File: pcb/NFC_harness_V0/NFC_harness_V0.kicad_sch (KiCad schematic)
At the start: 33 parts, among them J1 armed, J2 programmer, J3 Vin, J4 triggerd, J5 sender, J6 detector, J7 triggerd, Q1 MMBT3904, U1 ATtiny202-SS, U4 TPS613221ADBV

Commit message: initial commit - with tiny, will be changed to pico
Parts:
- removed C1, C2, C5, C9: 100n, Capacitor_SMD:C_0805_2012Metric, symbol Device:C
- removed C14: 4.7u, Capacitor_SMD:C_1206_3216Metric, symbol Device:C
- removed C3: 10u, Capacitor_SMD:C_0805_2012Metric, symbol Device:C
- removed D1, D2: LED, LED_SMD:LED_1206_3216Metric, symbol Device:LED
- removed J1: armed, Connector_PinHeader_2.54mm:PinHeader_1x02_P2.54mm_Vertical, symbol Connector:Conn_01x02_Pin
- removed J2: programmer, Connector_PinHeader_2.54mm:PinHeader_1x03_P2.54mm_Vertical, symbol Connector:Conn_01x03_Pin
- removed J4, J7: triggerd, Connector_PinHeader_2.54mm:PinHeader_1x02_P2.54mm_Vertical, symbol Connector:Conn_01x02_Pin
- removed J5: sender, Connector_PinHeader_2.54mm:PinHeader_1x03_P2.54mm_Vertical, symbol Connector:Conn_01x03_Pin
- removed J6: detector, Connector_PinHeader_2.54mm:PinHeader_1x03_P2.54mm_Vertical, symbol Connector:Conn_01x03_Pin
- removed L1: 6.8 uH, Inductor Coilcraft:L_Coilcraft_LPS4018, symbol Device:L
- removed Q1: MMBT3904, Package_TO_SOT_SMD:SOT-23, symbol Transistor_BJT:MMBT3904
- removed R1: 1k, Resistor_SMD:R_0805_2012Metric, symbol Device:R
- removed R11, R9: 470k, Resistor_SMD:R_0805_2012Metric, symbol Device:R
- removed R2, R3, R7: 220, Resistor_SMD:R_0805_2012Metric, symbol Device:R
- removed R4, R5: 100k, Resistor_SMD:R_0805_2012Metric, symbol Device:R
- removed R6: 1M, Resistor_SMD:R_0805_2012Metric, symbol Device:R
- removed U1: ATtiny202-SS, Package_SO:SOIC-8_3.9x4.9mm_P1.27mm, symbol MCU_Microchip_ATtiny:ATtiny202-SS
- removed U4: TPS613221ADBV, Package_TO_SOT_SMD:SOT-23-5, symbol Regulator_Switching:TPS613221ADBV
- added A1: RaspberryPi_Pico_W, Module_RaspberryPi_Pico:RaspberryPi_Pico_W_SMD, symbol MCU_Module_RaspberryPi_Pico:RaspberryPi_Pico_W_DebugPins
- added SW1: SW_DIP_x04, symbol Switch:SW_DIP_x04
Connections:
- new net: A1.13 (GND), A1.18 (GND), A1.23 (GND), A1.28 (GND), A1.3 (GND), A1.38 (GND), A1.8 (GND), A1.D2 (GND)

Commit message: pcb symbols st25
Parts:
- added IC1: ST25DV04KC-IE6S3, ST25DV04KC-IE6S3:SOIC127P600X175-8N, symbol ST25DV04KC-IE6S3:ST25DV04KC-IE6S3
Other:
- moved on the sheet: SW1
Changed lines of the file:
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@@
 	(symbol
 		(lib_id "Switch:SW_DIP_x04")
-		(at 135.89 119.38 0)
+		(at 189.23 96.52 0)
 		(unit 1)
 		(exclude_from_sim no)
@@
 		(fields_autoplaced yes)
 		(property "Reference" "SW1"
-			(at 135.89 106.68 0)
+			(at 189.23 83.82 0)
 			(effects
 				(font
@@
 		)
 		(property "Value" "SW_DIP_x04"
-			(at 135.89 109.22 0)
+			(at 189.23 86.36 0)
 			(effects
 				(font
@@
 		)
 		(property "Footprint" ""
-			(at 135.89 119.38 0)
+			(at 189.23 96.52 0)
 			(effects
 				(font
@@
 		)
 		(property "Datasheet" "~"
-			(at 135.89 119.38 0)
+			(at 189.23 96.52 0)
 			(effects
 				(font
@@
 		)
 		(property "Description" "4x DIP Switch, Single Pole Single Throw (SPST) switch, small symbol"
-			(at 135.89 119.38 0)
+			(at 189.23 96.52 0)
 			(effects
 				(font
@@
 					(unit 1)
 				)
+			)
+		)
+	)
+	(symbol
+		(lib_id "ST25DV04KC-IE6S3:ST25DV04KC-IE6S3")
+		(at 120.65 74.93 0)
+		(unit 1)
+		(exclude_from_sim no)
+		(in_bom yes)
+		(on_board yes)
+		(dnp no)
+		(fields_autoplaced yes)
+		(property "Reference" "IC1"
+			(at 142.24 67.31 0)
+			(effects
+				(font
+					(size 1.27 1.27)
+				)
+			)
+		)
+		(property "Value" "ST25DV04KC-IE6S3"
+			(at 142.24 69.85 0)
+			(effects
+				(font
+					(size 1.27 1.27)
+				)
+			)
+		)
+		(property "Footprint" "ST25DV04KC-IE6S3:SOIC127P600X175-8N"
+			(at 160.02 169.85 0)
+			(effects
+				(font
+					(size 1.27 1.27)
+				)
+				(justify left top)
+				(hide yes)
+			)
+		)
+		(property "Datasheet" "https://www.st.com/resource/en/datasheet/st25dv04kc.pdf"
+			(at 160.02 269.85 0)
+			(effects
+				(font
+					(size 1.27 1.27)
+				)
+				(justify left top)
+				(hide yes)
+			)
+		)
+		(property "Description" "Dynamic NFC/RFID tag IC with 4-, 16-, or 64-Kbit EEPROM, fast transfer mode capability, and optimized I2C"
+			(at 120.65 74.93 0)
+			(effects
+				(font
+					(size 1.27 1.27)
+				)
+				(hide yes)
+			)
+		)
+		(property "Height" "1.75"
+			(at 160.02 469.85 0)
+			(effects
+				(font
+					(size 1.27 1.27)
+				)
+				(justify left top)
+				(hide yes)
+			)
+		)
+		(property "Mouser Part Number" "511-ST25DV04KC-IE6S3"
+			(at 160.02 569.85 0)
+			(effects
+				(font
+					(size 1.27 1.27)
+				)
+				(justify left top)
+				(hide yes)
+			)
+		)
+		(property "Mouser Price/Stock" "https://www.mouser.co.uk/ProductDetail/STMicroelectronics/ST25DV04KC-IE6S3?qs=QNEnbhJQKvZQBnG6g7VtqA%3D%3D"
+			(at 160.02 669.85 0)
+			(effects
+				(font
+					(size 1.27 1.27)
+				)
+				(justify left top)
+				(hide yes)
+			)
+		)
+		(property "Manufacturer_Name" "STMicroelectronics"
+			(at 160.02 769.85 0)
+			(effects
+				(font
+					(size 1.27 1.27)
+				)
+				(justify left top)
+				(hide yes)
+			)
+		)
+		(property "Manufacturer_Part_Number" "ST25DV04KC-IE6S3"
+			(at 160.02 869.85 0)
+			(effects
+				(font
+					(size 1.27 1.27)
+				)
+				(justify left top)
+				(hide yes)
+			)
+		)
+		(pin "2"
+		)
+		(pin "1"
+		)
+		(pin "5"
+		)
+		(pin "3"
+		)
+		(pin "6"
+		)
+		(pin "7"
+		)
+		(pin "4"
+		)
+		(pin "8"
+		)
+		(instances
+			(project ""
+				(path "/c4720908-7c6f-4e13-a46e-cd0970db3513"
+					(reference "IC1")
+					(unit 1)
+				)

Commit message: pcb work
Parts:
- removed C4: 100n, Capacitor_SMD:C_0805_2012Metric, symbol Device:C
- removed C6: 10u, Capacitor_SMD:C_0805_2012Metric, symbol Device:C
- removed H1: MountingHole, MountingHole:MountingHole_2.1mm, symbol Mechanical:MountingHole
- removed R10, R8: 0, Resistor_SMD:R_1206_3216Metric, symbol Device:R
- removed SW1: SW_DIP_x04, symbol Switch:SW_DIP_x04
- added C1: 100n, Capacitor_SMD:C_0805_2012Metric, symbol Device:C
- added R1, R2: 4k7, Resistor_SMD:R_1206_3216Metric, symbol Device:R
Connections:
- net GND: now also A1.13 (GND), A1.18 (GND), A1.23 (GND), A1.28 (GND), A1.3 (GND), A1.33 (AGND), A1.38 (GND), A1.8 (GND), A1.D2 (GND), IC1.4 (VSS), C1.2; no longer J3.1 (Pin_1)
- net at J3.2 (Pin_2): now also IC1.3 (AC1)
- net at IC1.2 (AC0): now also J3.1 (Pin_1)
- net at IC1.5 (SDA): now also A1.26 (GPIO20), R1.2
- net at IC1.6 (SCL): now also A1.27 (GPIO21), R2.2
- net at IC1.7 (GPO_(OPEN_DRAIN)): now also A1.25 (GPIO19)
- net at IC1.8 (VCC): now also A1.24 (GPIO18), C1.1
- net at A1.36 (3V3): now also R1.1, R2.1
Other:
- moved on the sheet: IC1, J3

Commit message: cam job output
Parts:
- added C13, C4: 4.7u, Capacitor_SMD:C_1206_3216Metric, symbol Device:C
- added C2: 10p, Capacitor_SMD:C_0805_2012Metric, symbol Device:C
- added C3: JZ400, JZ400:JZ400, symbol JZ400:JZ400
- added J1: energy harvest, Connector_PinHeader_2.54mm:PinHeader_1x02_P2.54mm_Vertical, symbol Connector:Conn_01x02_Pin
- added R3: 0, Resistor_SMD:R_1206_3216Metric, symbol Device:R
- J3: value Vin -> antenna
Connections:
- net GND: now also C13.2, C4.2, J1.1 (Pin_1), R3.1, R3.2
- net at IC1.1 (V_EH): now also C13.1, J1.2 (Pin_2)
- net at IC1.2 (AC0), J3.1 (Pin_1): now also C2.2, C3.1
- net at IC1.3 (AC1), J3.2 (Pin_2): now also C2.1, C3.2
- net at A1.24 (GPIO18), C1.1, IC1.8 (VCC): now also C4.1
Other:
- moved on the sheet: J3

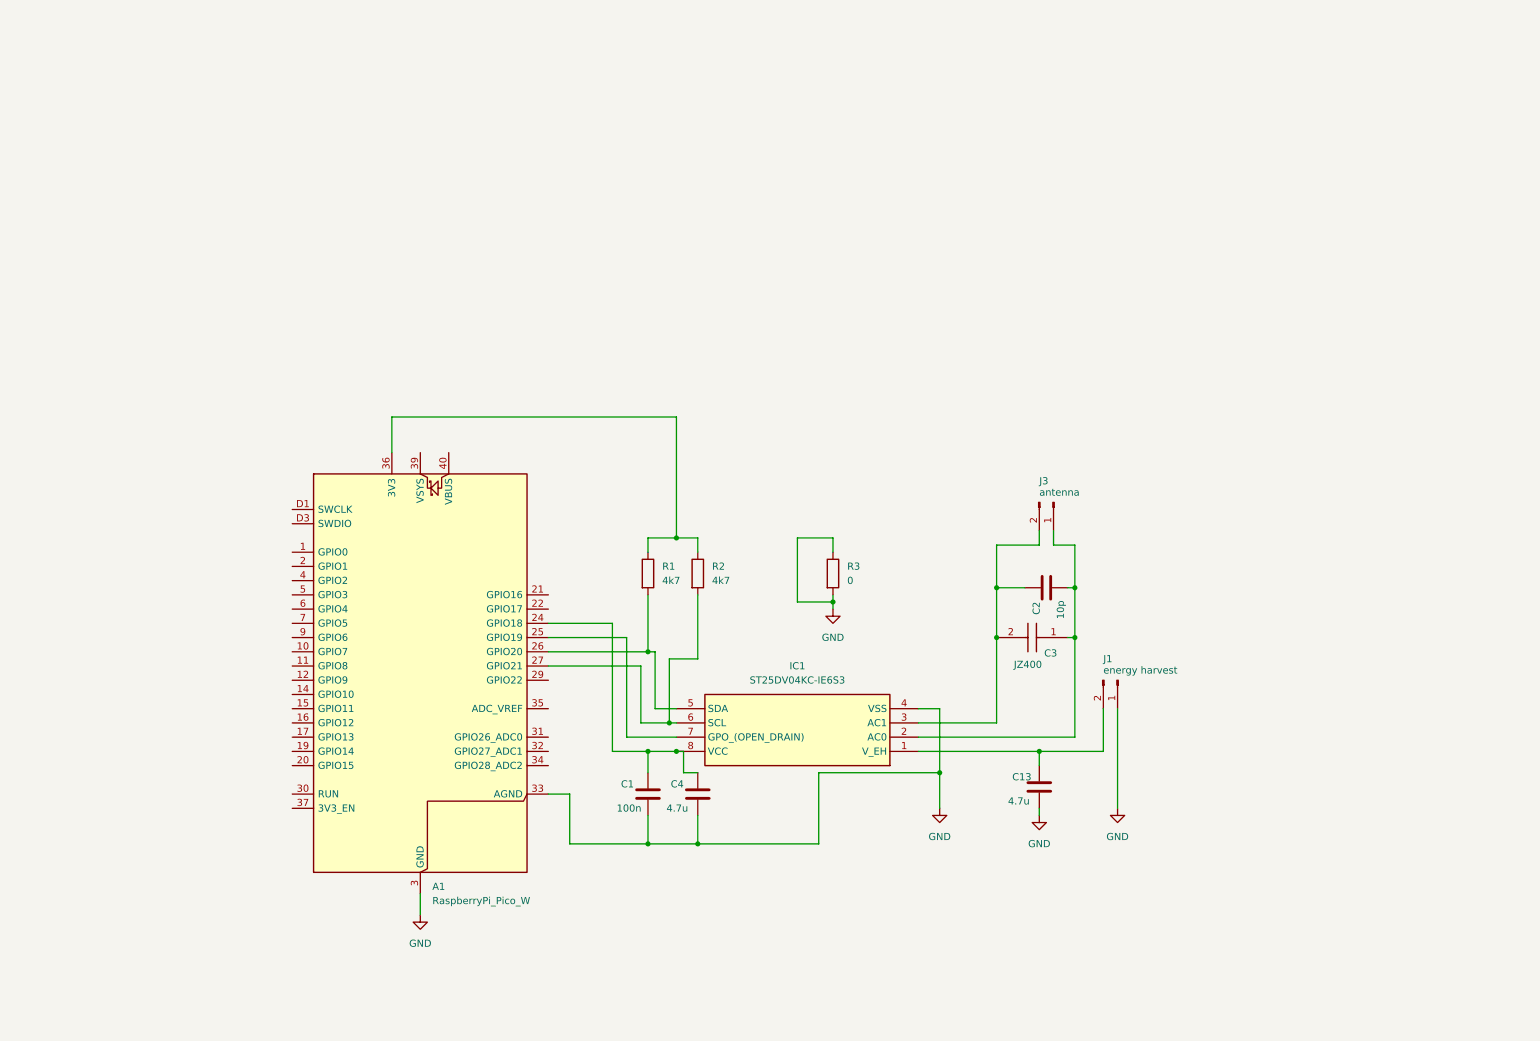
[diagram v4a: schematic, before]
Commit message: pcb: update NFC harness and add Taster 9313 footprint
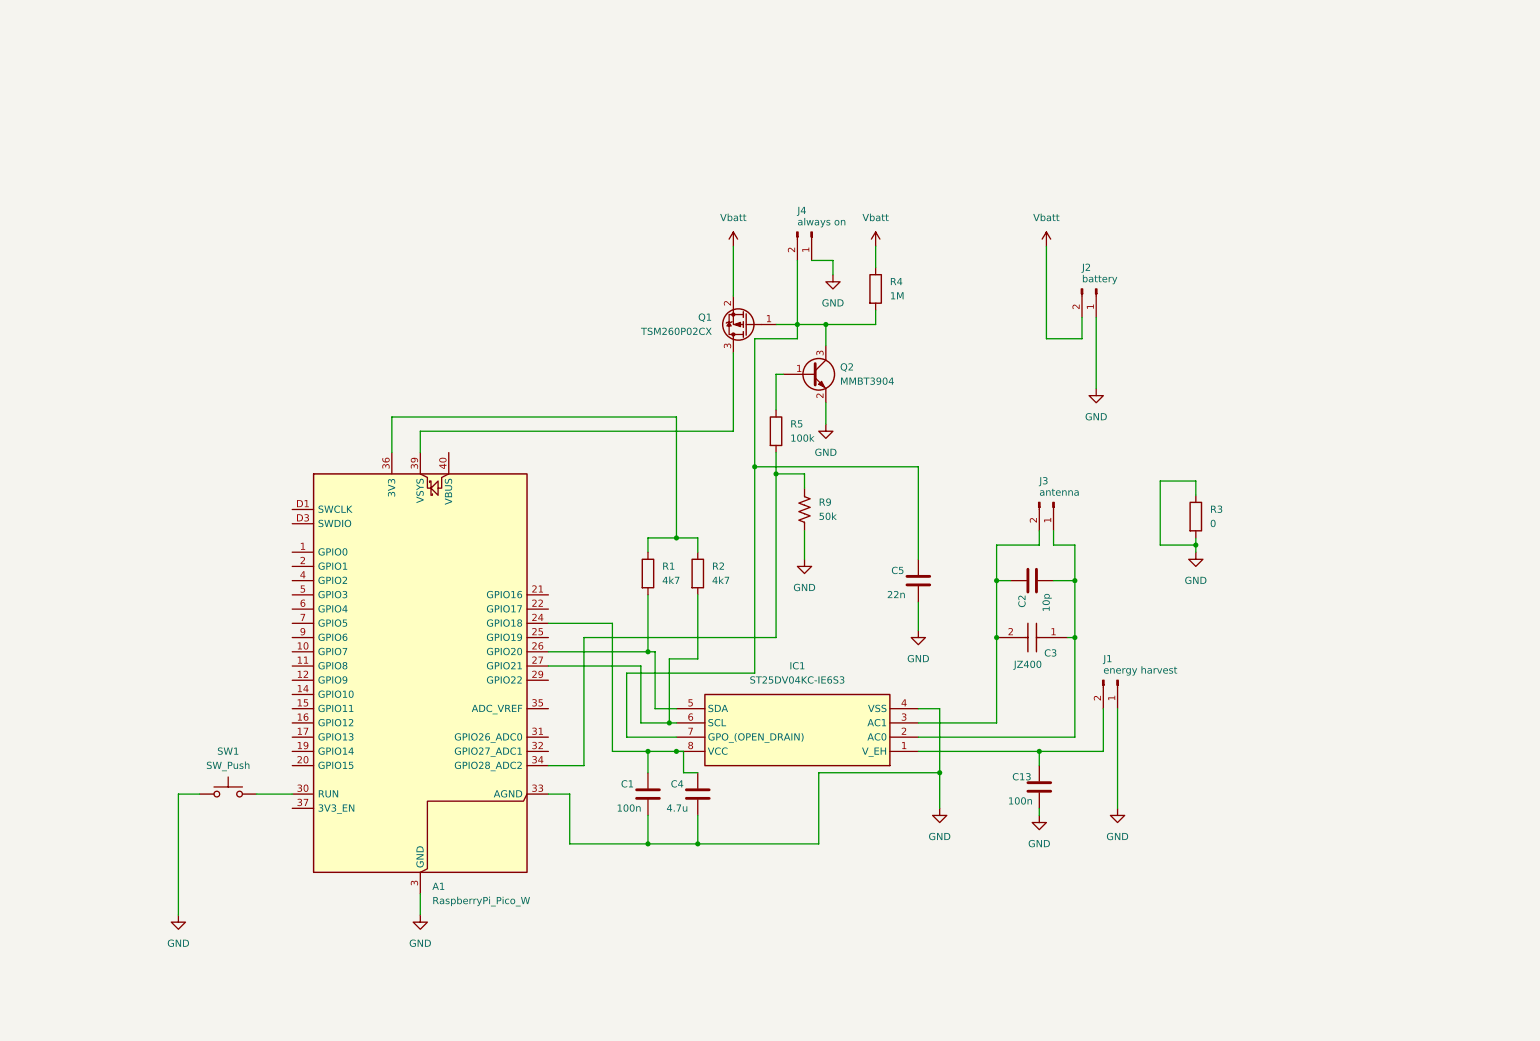
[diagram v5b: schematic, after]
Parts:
- added C5: 22n, Capacitor_SMD:C_0805_2012Metric, symbol Device:C
- added J2: battery, Connector_PinHeader_2.54mm:PinHeader_1x02_P2.54mm_Vertical, symbol Connector:Conn_01x02_Pin
- added J4: always on, Connector_PinHeader_2.54mm:PinHeader_1x02_P2.54mm_Vertical, symbol Connector:Conn_01x02_Pin
- added Q1: TSM260P02CX, Package_TO_SOT_SMD:SOT-23_Handsoldering, symbol Transistor_FET:TSM2301ACX
- added Q2: MMBT3904, Package_TO_SOT_SMD:SOT-23, symbol Transistor_BJT:MMBT3904
- added R4: 1M, Resistor_SMD:R_0805_2012Metric_Pad1.20x1.40mm_HandSolder, symbol Device:R
- added R5: 100k, Fuse:Fuse_1206_3216Metric_Pad1.42x1.75mm_HandSolder, symbol Device:R
- added R9: 50k, Fuse:Fuse_1206_3216Metric_Pad1.42x1.75mm_HandSolder, symbol Device:R_US
- added SW1: SW_Push, Taster:Taster 9313, symbol Switch:SW_Push
- C13: value 4.7u -> 100n; footprint Capacitor_SMD:C_1206_3216Metric -> Capacitor_SMD:C_0805_2012Metric
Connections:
- net GND: now also C5.2, J2.1 (Pin_1), J4.1 (Pin_1), Q2.2 (E), R9.2, SW1.1
- net at IC1.7 (GPO_(OPEN_DRAIN)): now also C5.1, J4.2 (Pin_2), Q1.1 (G), Q2.3 (C), R4.2; no longer A1.25 (GPIO19)
- net at A1.30 (RUN): now also SW1.2
- net at A1.34 (GPIO28_ADC2): now also R5.2, R9.1
- net at A1.39 (VSYS): now also Q1.3 (D)
- new net: Q2.1 (B), R5.1
- new net Vbatt: J2.2 (Pin_2), Q1.2 (S), R4.1
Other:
- moved on the sheet: C2, R3

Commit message: pcb edits
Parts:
- added R6: 0, Fuse:Fuse_1206_3216Metric_Pad1.42x1.75mm_HandSolder, symbol Device:R
- R1, R2, R3: footprint Resistor_SMD:R_1206_3216Metric -> Fuse:Fuse_1206_3216Metric_Pad1.42x1.75mm_HandSolder
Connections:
- net GND: now also R6.1, R6.2
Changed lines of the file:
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@@
 	)
 	(junction
+		(at 227.33 97.79)
+		(diameter 0)
+		(color 0 0 0 0)
+	)
+	(junction
 		(at 191.77 125.73)
 		(diameter 0)
@@
 	(wire
 		(pts
+			(xy 234.95 100.33) (xy 234.95 97.79)
+		)
+		(stroke
+			(width 0)
+			(type default)
+		)
+	)
+	(wire
+		(pts
 			(xy 138.43 162.56) (xy 160.02 162.56)
 		)
@@
 	(wire
 		(pts
+			(xy 227.33 109.22) (xy 234.95 109.22)
+		)
+		(stroke
+			(width 0)
+			(type default)
+		)
+	)
+	(wire
+		(pts
 			(xy 59.69 153.67) (xy 66.04 153.67)
 		)
@@
 	(wire
 		(pts
+			(xy 234.95 97.79) (xy 227.33 97.79)
+		)
+		(stroke
+			(width 0)
+			(type default)
+		)
+	)
+	(wire
+		(pts
 			(xy 161.29 83.82) (xy 161.29 87.63)
 		)
@@
 	(wire
 		(pts
+			(xy 234.95 109.22) (xy 234.95 107.95)
+		)
+		(stroke
+			(width 0)
+			(type default)
+		)
+	)
+	(wire
+		(pts
 			(xy 130.81 128.27) (xy 130.81 138.43)
 		)
@@
 			)
 		)
-		(property "Footprint" "Resistor_SMD:R_1206_3216Metric"
+		(property "Footprint" "Fuse:Fuse_1206_3216Metric_Pad1.42x1.75mm_HandSolder"
 			(at 225.552 104.14 90)
 			(effects
@@
 			)
 		)
-		(property "Footprint" "Resistor_SMD:R_1206_3216Metric"
+		(property "Footprint" "Fuse:Fuse_1206_3216Metric_Pad1.42x1.75mm_HandSolder"
 			(at 136.652 114.3 90)
 			(effects
@@
 	)
 	(symbol
+		(lib_id "Device:R")
+		(at 234.95 104.14 0)
+		(unit 1)
+		(exclude_from_sim no)
+		(in_bom yes)
+		(on_board yes)
+		(dnp no)
+		(fields_autoplaced yes)
+		(property "Reference" "R6"
+			(at 237.49 102.8699 0)
+			(effects
+				(font
+					(size 1.27 1.27)
+				)
+				(justify left)
+			)
+		)
+		(property "Value" "0"
+			(at 237.49 105.4099 0)
+			(effects
+				(font
+					(size 1.27 1.27)
+				)
+				(justify left)
+			)
+		)
+		(property "Footprint" "Fuse:Fuse_1206_3216Metric_Pad1.42x1.75mm_HandSolder"
+			(at 233.172 104.14 90)
+			(effects
+				(font
+					(size 1.27 1.27)
+				)
+				(hide yes)
+			)
+		)
+		(property "Datasheet" "~"
+			(at 234.95 104.14 0)
+			(effects
+				(font
+					(size 1.27 1.27)
+				)
+				(hide yes)
+			)
+		)
+		(property "Description" "Resistor"
+			(at 234.95 104.14 0)
+			(effects
+				(font
+					(size 1.27 1.27)
+				)
+				(hide yes)
+			)
+		)
+		(pin "2"
+		)
+		(pin "1"
+		)
+		(instances
+			(project "NFC_harness_V0"
+				(path "/c4720908-7c6f-4e13-a46e-cd0970db3513"
+					(reference "R6")
+					(unit 1)
+				)
+			)
+		)
+	)
+	(symbol
 		(lib_id "power:GND")
 		(at 213.36 156.21 0)
@@
 			)
 		)
-		(property "Footprint" "Resistor_SMD:R_1206_3216Metric"
+		(property "Footprint" "Fuse:Fuse_1206_3216Metric_Pad1.42x1.75mm_HandSolder"
 			(at 127.762 114.3 90)
 			(effects
